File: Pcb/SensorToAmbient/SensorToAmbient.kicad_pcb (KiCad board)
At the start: 2 copper layers, 161.9 x 69.7 mm, 14 parts, among them J1 Conn_01x04, J2 Conn_01x04, J3 Conn_01x04, J4 Conn_01x04, J5 Conn_01x04, J6 Conn_01x04, J7 Conn_01x02, J8 Conn_01x06, J9 Conn_01x06

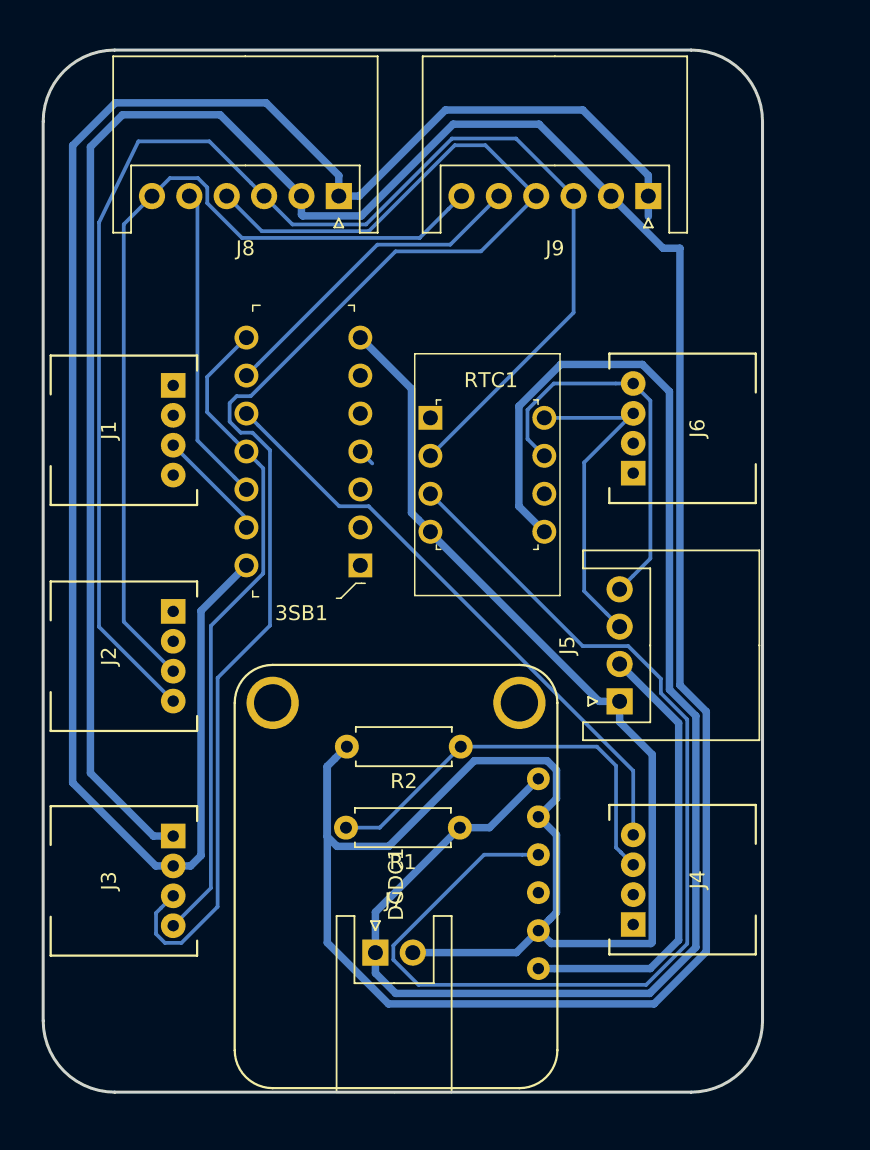
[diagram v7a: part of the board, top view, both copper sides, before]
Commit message: Make ground plane
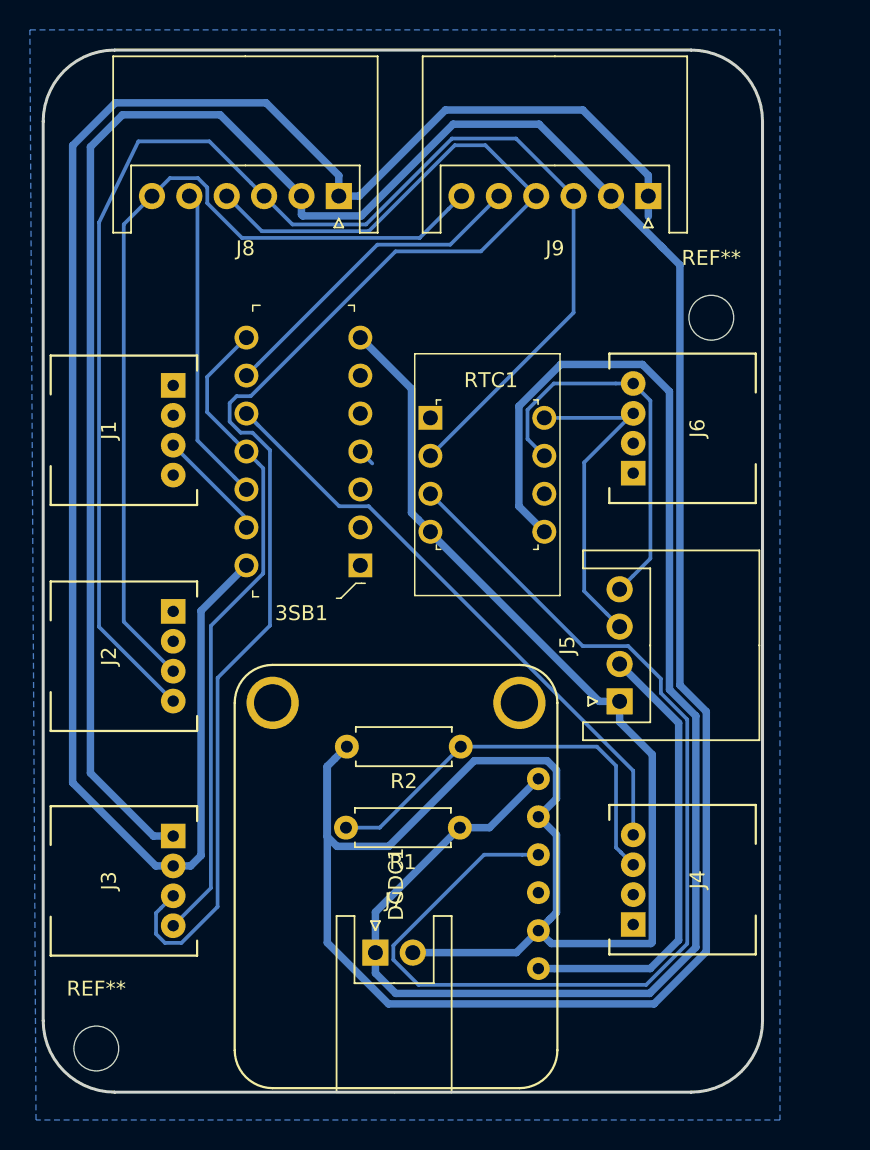
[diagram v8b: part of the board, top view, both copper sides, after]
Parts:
- added REF**: MountingHole_3mm, Mounting_Holes:MountingHole_3mm, F.Cu at (26.2, 84.6)
- added REF**: MountingHole_3mm, Mounting_Holes:MountingHole_3mm, F.Cu at (67.4, 35.7)
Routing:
- net Net-(3SB1-Pad10): track 40.1 -> 41.2 mm
- added copper zone on B.Cu, net GND
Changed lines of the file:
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@@
     (thickness 1.6)
     (drawings 16)
-    (tracks 197)
+    (tracks 198)
     (zones 0)
-    (modules 14)
+    (modules 16)
     (nets 35)
   )
@@
     )
   )
+  (module Mounting_Holes:MountingHole_3mm (layer F.Cu)
+    (at 26.2233 84.586)
+    (descr "Mounting Hole 3mm, no annular")
+    (tags "mounting hole 3mm no annular")
+    (attr virtual)
+    (fp_text reference REF** (at 0 -4) (layer F.SilkS)
+      (effects (font (size 1 1) (thickness 0.15)))
+    )
+    (fp_text value MountingHole_3mm (at 0 4) (layer F.Fab)
+      (effects (font (size 1 1) (thickness 0.15)))
+    )
+    (fp_text user %R (at 0.3 0) (layer F.Fab)
+      (effects (font (size 1 1) (thickness 0.15)))
+    )
+    (fp_circle (center 0 0) (end 3 0) (layer Cmts.User) (width 0.15))
+    (fp_circle (center 0 0) (end 3.25 0) (layer F.CrtYd) (width 0.05))
+    (pad 1 np_thru_hole circle (at 0 0) (size 3 3) (drill 3) (layers *.Cu *.Mask))
+  )
+  (module Mounting_Holes:MountingHole_3mm (layer F.Cu)
+    (at 67.374 35.691)
+    (descr "Mounting Hole 3mm, no annular")
+    (tags "mounting hole 3mm no annular")
+    (attr virtual)
+    (fp_text reference REF** (at 0 -4) (layer F.SilkS)
+      (effects (font (size 1 1) (thickness 0.15)))
+    )
+    (fp_text value MountingHole_3mm (at 0 4) (layer F.Fab)
+      (effects (font (size 1 1) (thickness 0.15)))
+    )
+    (fp_text user %R (at 0.3 0) (layer F.Fab)
+      (effects (font (size 1 1) (thickness 0.15)))
+    )
+    (fp_circle (center 0 0) (end 3 0) (layer Cmts.User) (width 0.15))
+    (fp_circle (center 0 0) (end 3.25 0) (layer F.CrtYd) (width 0.05))
+    (pad 1 np_thru_hole circle (at 0 0) (size 3 3) (drill 3) (layers *.Cu *.Mask))
+  )
   (gr_arc (start 179.823 75.947) (end 179.823 80.727) (angle -90) (layer Edge.Cuts) (width 0.2))
   (gr_line (start 141.25 80.727) (end 179.823 80.727) (layer Edge.Cuts) (width 0.2))
@@
   (segment (start 45.790001 71.060001) (end 42.329999 71.060001) (width 0.5) (layer B.Cu) (net 6))
   (segment (start 55.805 69.0795) (end 57.017001 67.867499) (width 0.5) (layer B.Cu) (net 6))
-  (segment (start 30.203274 72.37) (end 24.64 66.806726) (width 0.5) (layer B.Cu) (net 11))
-  (segment (start 31.37 72.37) (end 30.203274 72.37) (width 0.5) (layer B.Cu) (net 11))
-  (segment (start 24.64 66.806726) (end 24.64 24.17) (width 0.5) (layer B.Cu) (net 11))
-  (segment (start 24.64 24.17) (end 27.5 21.31) (width 0.5) (layer B.Cu) (net 11))
-  (segment (start 42.45 26.175) (end 42.45 27.55) (width 0.5) (layer B.Cu) (net 11))
-  (segment (start 37.585 21.31) (end 42.45 26.175) (width 0.5) (layer B.Cu) (net 11))
-  (segment (start 27.5 21.31) (end 37.585 21.31) (width 0.5) (layer B.Cu) (net 11))
-  (segment (start 43.825 27.55) (end 49.585 21.79) (width 0.5) (layer B.Cu) (net 11))
-  (segment (start 42.45 27.55) (end 43.825 27.55) (width 0.5) (layer B.Cu) (net 11))
-  (segment (start 63.16 26.175) (end 63.16 27.55) (width 0.5) (layer B.Cu) (net 11))
-  (segment (start 58.775 21.79) (end 63.16 26.175) (width 0.5) (layer B.Cu) (net 11))
-  (segment (start 49.585 21.79) (end 58.775 21.79) (width 0.5) (layer B.Cu) (net 11))
   (segment (start 42.190001 65.189999) (end 42.99 64.39) (width 0.5) (layer B.Cu) (net 6))
   (segment (start 41.679999 65.700001) (end 42.190001 65.189999) (width 0.5) (layer B.Cu) (net 6))
-  (segment (start 63.16 27.55) (end 63.16 28.925) (width 0.5) (layer B.Cu) (net 11))
   (segment (start 41.679999 77.510001) (end 41.679999 65.700001) (width 0.5) (layer B.Cu) (net 6))
   (segment (start 45.771519 81.601521) (end 41.679999 77.510001) (width 0.5) (layer B.Cu) (net 6))
@@
   (segment (start 67.04003 78.10631) (end 63.544819 81.601521) (width 0.5) (layer B.Cu) (net 6))
   (segment (start 65.275031 60.278691) (end 67.040031 62.043694) (width 0.5) (layer B.Cu) (net 6))
-  (segment (start 65.275031 31.040031) (end 65.275031 60.278691) (width 0.5) (layer B.Cu) (net 6))
   (segment (start 67.040031 62.043694) (end 67.04003 78.10631) (width 0.5) (layer B.Cu) (net 6))
   (segment (start 47.780001 49.210001) (end 48.58 50.01) (width 0.5) (layer B.Cu) (net 6))
@@
   (segment (start 47.311512 40.441512) (end 47.311512 48.741512) (width 0.5) (layer B.Cu) (net 6))
   (segment (start 43.89 37.02) (end 47.311512 40.441512) (width 0.5) (layer B.Cu) (net 6))
-  (segment (start 64.150031 31.040031) (end 60.66 27.55) (width 0.5) (layer B.Cu) (net 6))
-  (segment (start 65.275031 31.040031) (end 64.150031 31.040031) (width 0.5) (layer B.Cu) (net 6))
   (segment (start 54.3345 78.17) (end 55.805 76.6995) (width 0.5) (layer B.Cu) (net 6))
   (segment (start 56.566999 77.461499) (end 55.805 76.6995) (width 0.5) (layer B.Cu) (net 6))
@@
   (segment (start 30.045 70.37) (end 31.37 70.37) (width 0.5) (layer B.Cu) (net 6))
   (segment (start 25.83 66.155) (end 30.045 70.37) (width 0.5) (layer B.Cu) (net 6))
+  (segment (start 65.275031 32.165031) (end 64.02 30.91) (width 0.5) (layer B.Cu) (net 6))
+  (segment (start 65.275031 60.278691) (end 65.275031 32.165031) (width 0.5) (layer B.Cu) (net 6))
+  (segment (start 64.150031 31.040031) (end 64.02 30.91) (width 0.5) (layer B.Cu) (net 6))
+  (segment (start 64.02 30.91) (end 60.66 27.55) (width 0.5) (layer B.Cu) (net 6))
   (segment (start 37.069999 42.899999) (end 36.27 42.1) (width 0.25) (layer B.Cu) (net 7))
-  (segment (start 42.475001 48.305001) (end 37.069999 42.899999) (width 0.25) (layer B.Cu) (net 7))
+  (segment (start 42.475001 48.305001) (end 36.27 42.1) (width 0.25) (layer B.Cu) (net 7))
   (segment (start 44.451503 48.305001) (end 42.475001 48.305001) (width 0.25) (layer B.Cu) (net 7))
   (segment (start 62.15 66.003498) (end 44.451503 48.305001) (width 0.25) (layer B.Cu) (net 7))
@@
   (segment (start 36.27 49.12) (end 36.27 49.72) (width 0.25) (layer B.Cu) (net 10))
   (segment (start 31.37 44.22) (end 36.27 49.12) (width 0.25) (layer B.Cu) (net 10))
+  (segment (start 30.203274 72.37) (end 24.64 66.806726) (width 0.5) (layer B.Cu) (net 11))
+  (segment (start 31.37 72.37) (end 30.203274 72.37) (width 0.5) (layer B.Cu) (net 11))
+  (segment (start 24.64 66.806726) (end 24.64 24.17) (width 0.5) (layer B.Cu) (net 11))
+  (segment (start 24.64 24.17) (end 27.5 21.31) (width 0.5) (layer B.Cu) (net 11))
+  (segment (start 42.45 26.175) (end 42.45 27.55) (width 0.5) (layer B.Cu) (net 11))
+  (segment (start 37.585 21.31) (end 42.45 26.175) (width 0.5) (layer B.Cu) (net 11))
+  (segment (start 27.5 21.31) (end 37.585 21.31) (width 0.5) (layer B.Cu) (net 11))
+  (segment (start 43.825 27.55) (end 49.585 21.79) (width 0.5) (layer B.Cu) (net 11))
+  (segment (start 42.45 27.55) (end 43.825 27.55) (width 0.5) (layer B.Cu) (net 11))
+  (segment (start 63.16 26.175) (end 63.16 27.55) (width 0.5) (layer B.Cu) (net 11))
+  (segment (start 58.775 21.79) (end 63.16 26.175) (width 0.5) (layer B.Cu) (net 11))
+  (segment (start 49.585 21.79) (end 58.775 21.79) (width 0.5) (layer B.Cu) (net 11))
+  (segment (start 63.16 27.55) (end 63.16 28.925) (width 0.5) (layer B.Cu) (net 11))
   (segment (start 32.536726 72.37) (end 31.37 72.37) (width 0.5) (layer B.Cu) (net 11))
   (segment (start 33.23 71.676726) (end 32.536726 72.37) (width 0.5) (layer B.Cu) (net 11))
@@
   (segment (start 49.909961 30.800039) (end 45.029961 30.800039) (width 0.25) (layer B.Cu) (net 33))
   (segment (start 53.16 27.55) (end 49.909961 30.800039) (width 0.25) (layer B.Cu) (net 33))
+  (zone (net 6) (net_name GND) (layer B.Cu) (hatch edge 0.508)
+    (connect_pads (clearance 0.508))
+    (min_thickness 0.254)
+    (fill yes (arc_segments 16) (thermal_gap 0.508) (thermal_bridge_width 0.508))
+    (polygon
+      (pts
+        (xy 21.78 16.43) (xy 71.97 16.43) (xy 71.97 89.37) (xy 22.19 89.37)
+      )
+    )
+  )
 )
